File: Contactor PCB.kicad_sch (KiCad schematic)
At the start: 21 parts, among them J1 TSCU, J2 TSCU, J3 IMD, J4 AIL, J5 UIL, J6 TBD, J7 To Precharge, U1 Gigavac_GX21CAB, U2 Gigavac_GX21CAB

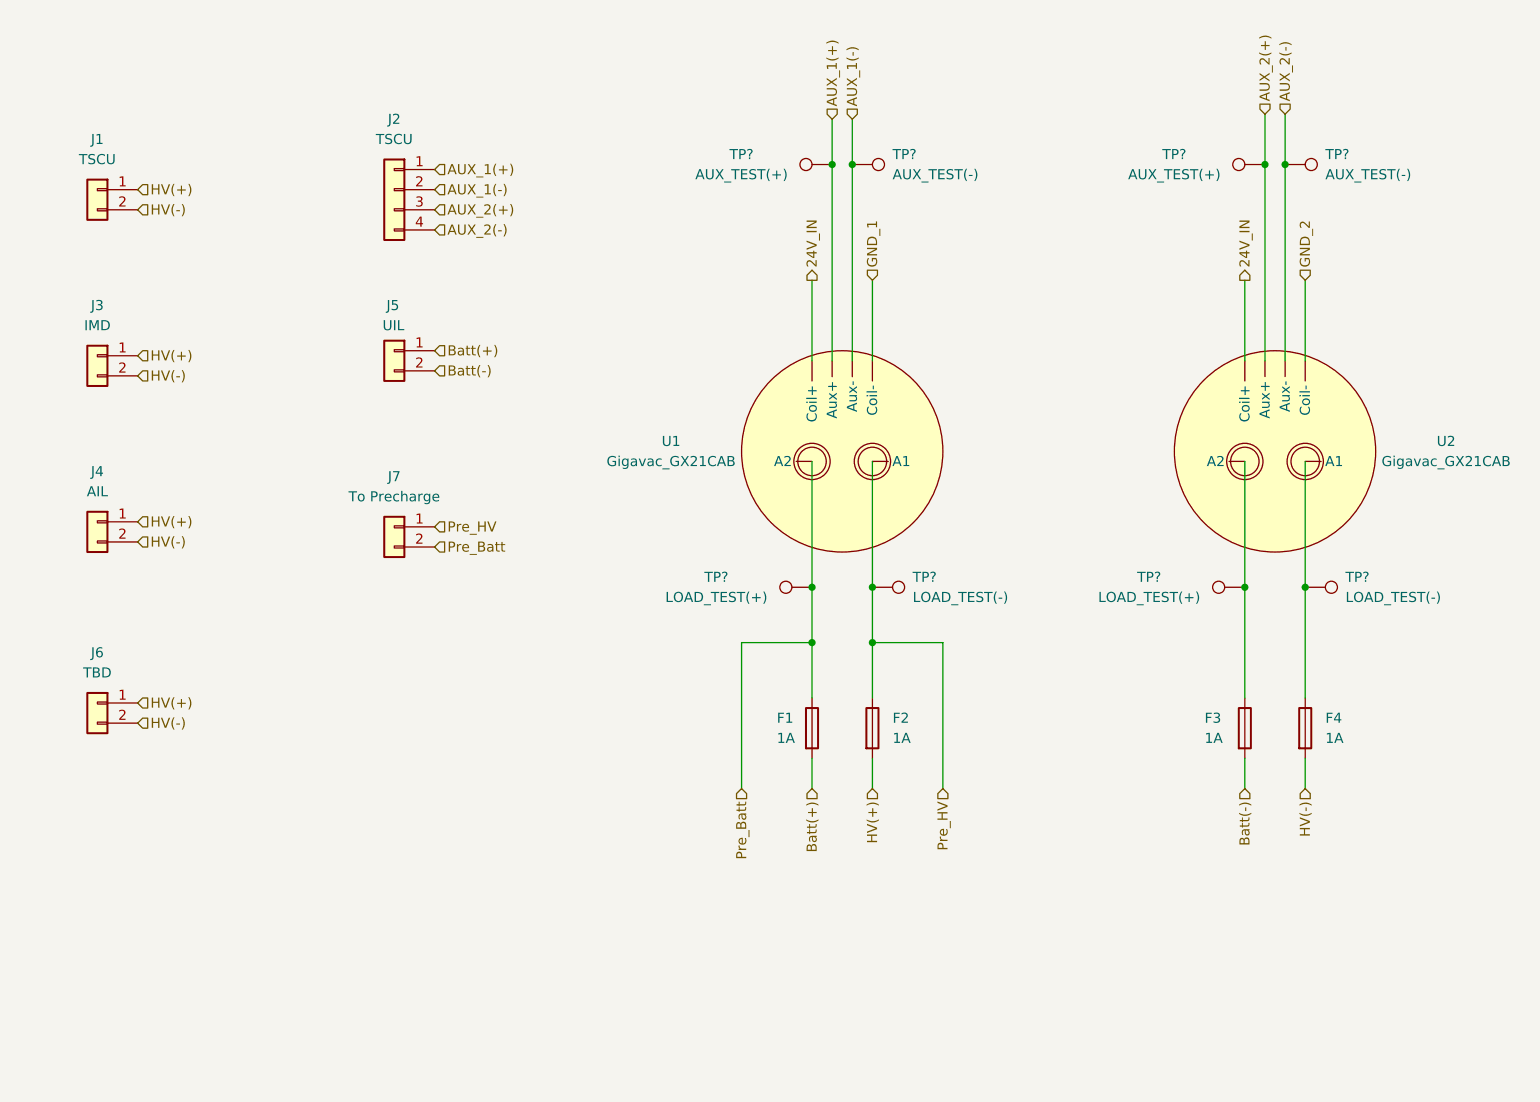
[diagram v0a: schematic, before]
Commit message: Added layout first draft
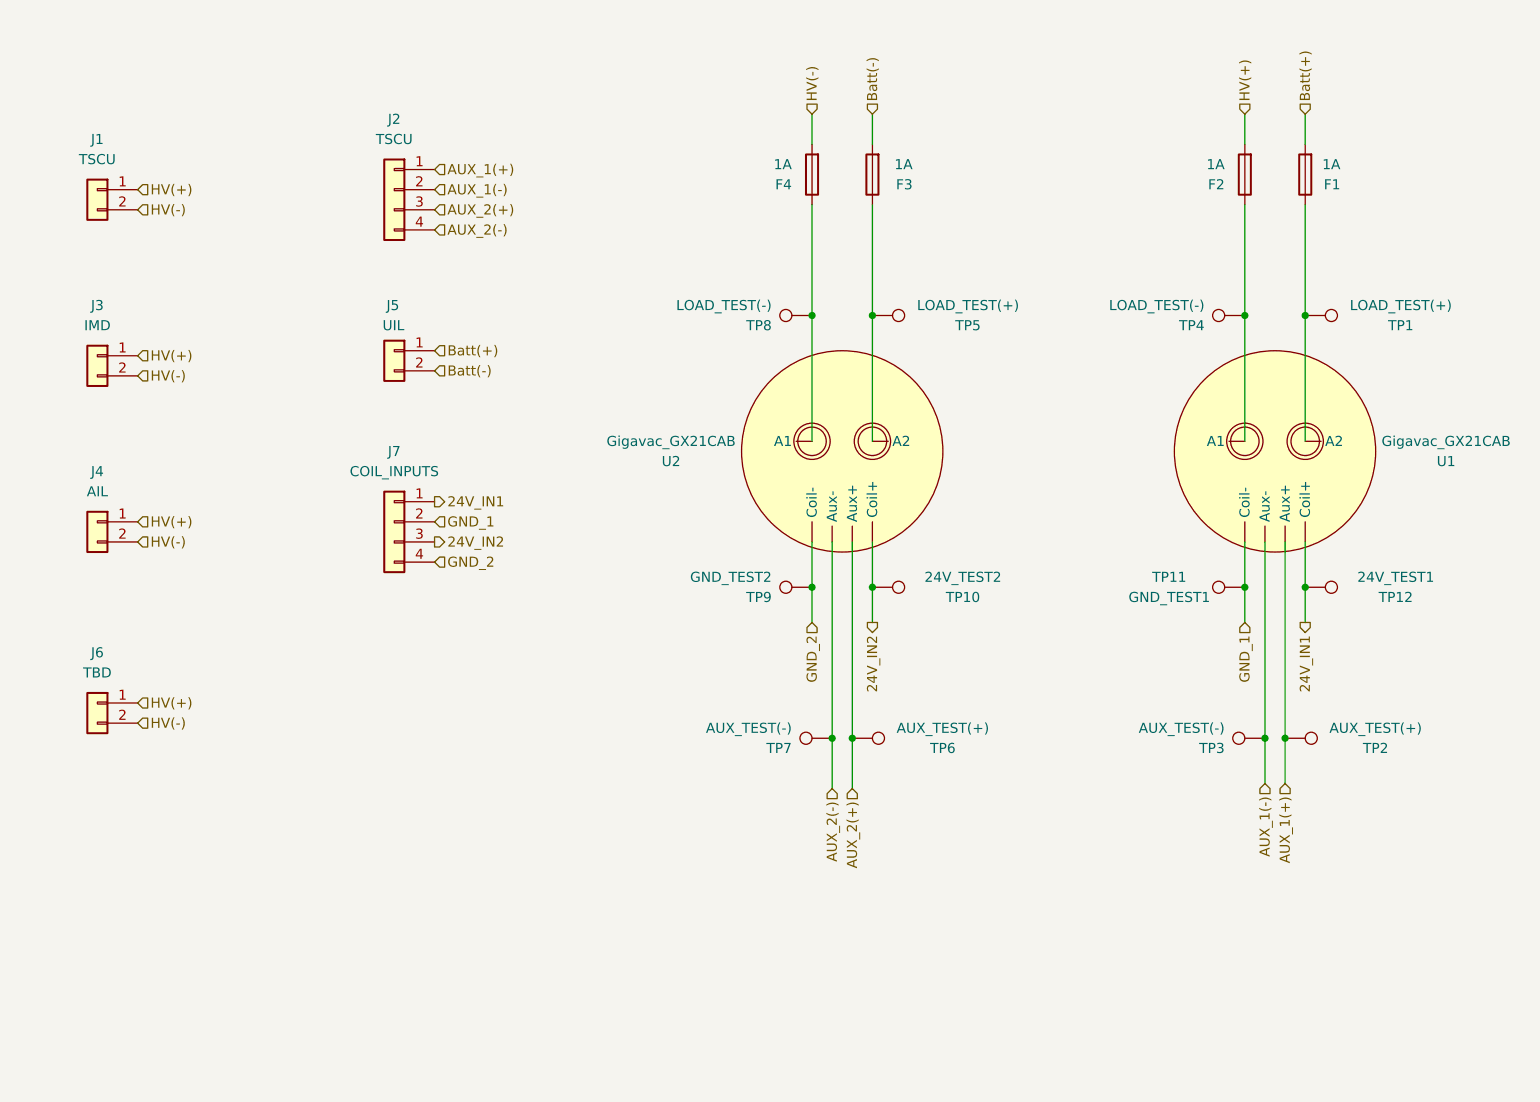
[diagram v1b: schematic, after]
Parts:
- removed J7: To Precharge, Connector_Molex:Molex_Micro-Fit_3.0_43045-0200_2x01_P3.00mm_Horizontal, symbol Connector_Generic:Conn_01x02
- added J7: COIL_INPUTS, Connector_Molex:Molex_Micro-Fit_3.0_43045-0400_2x02_P3.00mm_Horizontal, symbol Connector_Generic:Conn_01x04
- added TP10: 24V_TEST2, TestPoint:TestPoint_THTPad_D1.0mm_Drill0.5mm, symbol Connector:TestPoint
- added TP11: GND_TEST1, TestPoint:TestPoint_THTPad_D1.0mm_Drill0.5mm, symbol Connector:TestPoint
- added TP12: 24V_TEST1, TestPoint:TestPoint_THTPad_D1.0mm_Drill0.5mm, symbol Connector:TestPoint
- added TP9: GND_TEST2, TestPoint:TestPoint_THTPad_D1.0mm_Drill0.5mm, symbol Connector:TestPoint
- J1: footprint Connector_Molex:Molex_Micro-Fit_3.0_43045-0600_2x03_P3.00mm_Horizontal -> Connector_Molex:Molex_Micro-Fit_3.0_43045-0200_2x01_P3.00mm_Horizontal
- TP1, TP2, TP3, TP4, TP5, TP6, TP7, TP8: renamed from TP?; footprint (none) -> TestPoint:TestPoint_THTPad_D1.0mm_Drill0.5mm
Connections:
- net GND_1: now also J7.2 (Pin_2), TP11.1
- net GND_2: now also J7.4 (Pin_4), TP9.1
- removed net 24V_IN: U1. (Coil-), U2. (Coil-)
- net Pre_Batt: no longer names the net of F1.1, TP1.1, U1. (Coil-)
- net Pre_HV: no longer names the net of F2.1, TP4.1, U1. (Coil-)
- new net 24V_IN1: J7.1 (Pin_1), TP12.1, U1. (Coil-)
- new net 24V_IN2: J7.3 (Pin_3), TP10.1, U2. (Coil-)
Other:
- moved on the sheet: F1, F2, F3, F4, TP1, TP2, TP3, TP4, TP5, TP6, TP7, TP8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

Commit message: Condensed Version
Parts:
- added J10: COIL2_CONNECTOR, Connector_Molex:Molex_Micro-Fit_3.0_43045-0212_2x01_P3.00mm_Vertical, symbol Connector_Generic:Conn_01x02
- added J11: AUX2_CONNECTOR, Connector_Molex:Molex_Micro-Fit_3.0_43045-0212_2x01_P3.00mm_Vertical, symbol Connector_Generic:Conn_01x02
- added J8: COIL1_CONNECTOR, Connector_Molex:Molex_Micro-Fit_3.0_43045-0212_2x01_P3.00mm_Vertical, symbol Connector_Generic:Conn_01x02
- added J9: AUX1_CONNECTOR, Connector_Molex:Molex_Micro-Fit_3.0_43045-0212_2x01_P3.00mm_Vertical, symbol Connector_Generic:Conn_01x02
- J1, J3, J4, J5, J6: footprint Connector_Molex:Molex_Micro-Fit_3.0_43045-0200_2x01_P3.00mm_Horizontal -> Connector_Molex:Molex_Micro-Fit_3.0_43045-0212_2x01_P3.00mm_Vertical
- J2, J7: footprint Connector_Molex:Molex_Micro-Fit_3.0_43045-0400_2x02_P3.00mm_Horizontal -> Connector_Molex:Molex_Micro-Fit_3.0_43045-0412_2x02_P3.00mm_Vertical
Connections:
- net 24V_IN1: now also J8.1 (Pin_1)
- net 24V_IN2: now also J10.1 (Pin_1)
- net AUX_1(+): now also J9.1 (Pin_1)
- net AUX_1(-): now also J9.2 (Pin_2)
- net AUX_2(+): now also J11.1 (Pin_1)
- net AUX_2(-): now also J11.2 (Pin_2)
- net Batt(+): now also J5.2 (Pin_2); no longer J5.1 (Pin_1)
- net Batt(-): now also J5.1 (Pin_1); no longer J5.2 (Pin_2)
- net GND_1: now also J8.2 (Pin_2)
- net GND_2: now also J10.2 (Pin_2)
- net HV(+): now also J1.2 (Pin_2), J3.2 (Pin_2), J4.2 (Pin_2), J6.2 (Pin_2); no longer J1.1 (Pin_1), J3.1 (Pin_1), J4.1 (Pin_1), J6.1 (Pin_1)
- net HV(-): now also J1.1 (Pin_1), J3.1 (Pin_1), J4.1 (Pin_1), J6.1 (Pin_1); no longer J1.2 (Pin_2), J3.2 (Pin_2), J4.2 (Pin_2), J6.2 (Pin_2)
- net at F4.1, TP8.1: now also U2.1 (A1); no longer U2. (Coil-)
- net at F3.1, TP5.1: now also U2.2 (A2); no longer U2. (Coil-)
- net at F2.1, TP4.1: now also U1.1 (A1); no longer U1. (Coil-)
- net at F1.1, TP1.1: now also U1.2 (A2); no longer U1. (Coil-)

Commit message: Finalize Board
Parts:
- removed J1: TSCU, Connector_Molex:Molex_Micro-Fit_3.0_43045-0212_2x01_P3.00mm_Vertical, symbol Connector_Generic:Conn_01x02
- removed J10: COIL2_CONNECTOR, Connector_Molex:Molex_Micro-Fit_3.0_43045-0212_2x01_P3.00mm_Vertical, symbol Connector_Generic:Conn_01x02
- removed J11: AUX2_CONNECTOR, Connector_Molex:Molex_Micro-Fit_3.0_43045-0212_2x01_P3.00mm_Vertical, symbol Connector_Generic:Conn_01x02
- removed J2: TSCU, Connector_Molex:Molex_Micro-Fit_3.0_43045-0412_2x02_P3.00mm_Vertical, symbol Connector_Generic:Conn_01x04
- removed J3: IMD, Connector_Molex:Molex_Micro-Fit_3.0_43045-0212_2x01_P3.00mm_Vertical, symbol Connector_Generic:Conn_01x02
- removed J4: AIL, Connector_Molex:Molex_Micro-Fit_3.0_43045-0212_2x01_P3.00mm_Vertical, symbol Connector_Generic:Conn_01x02
- removed J5: UIL, Connector_Molex:Molex_Micro-Fit_3.0_43045-0212_2x01_P3.00mm_Vertical, symbol Connector_Generic:Conn_01x02
- removed J6: TBD, Connector_Molex:Molex_Micro-Fit_3.0_43045-0212_2x01_P3.00mm_Vertical, symbol Connector_Generic:Conn_01x02
- removed J7: COIL_INPUTS, Connector_Molex:Molex_Micro-Fit_3.0_43045-0412_2x02_P3.00mm_Vertical, symbol Connector_Generic:Conn_01x04
- removed J8: COIL1_CONNECTOR, Connector_Molex:Molex_Micro-Fit_3.0_43045-0212_2x01_P3.00mm_Vertical, symbol Connector_Generic:Conn_01x02
- removed J9: AUX1_CONNECTOR, Connector_Molex:Molex_Micro-Fit_3.0_43045-0212_2x01_P3.00mm_Vertical, symbol Connector_Generic:Conn_01x02
- removed TP10: 24V_TEST2, TestPoint:TestPoint_THTPad_D1.0mm_Drill0.5mm, symbol Connector:TestPoint
- removed TP11: GND_TEST1, TestPoint:TestPoint_THTPad_D1.0mm_Drill0.5mm, symbol Connector:TestPoint
- removed TP12: 24V_TEST1, TestPoint:TestPoint_THTPad_D1.0mm_Drill0.5mm, symbol Connector:TestPoint
- removed TP2, TP6: AUX_TEST(+), TestPoint:TestPoint_THTPad_D1.0mm_Drill0.5mm, symbol Connector:TestPoint
- removed TP3, TP7: AUX_TEST(-), TestPoint:TestPoint_THTPad_D1.0mm_Drill0.5mm, symbol Connector:TestPoint
- removed TP9: GND_TEST2, TestPoint:TestPoint_THTPad_D1.0mm_Drill0.5mm, symbol Connector:TestPoint
- added J1: HV Connector, Connector_Molex:Molex_Micro-Fit_3.0_43045-1012_2x05_P3.00mm_Vertical, symbol Connector_Generic:Conn_02x05_Top_Bottom
- added J2: Batt Connector, Connector_Molex:Molex_Micro-Fit_3.0_43045-0612_2x03_P3.00mm_Vertical, symbol Connector_Generic:Conn_02x03_Top_Bottom
- F1, F2, F3, F4: footprint CustomFootprints:Fuse_Placeholder -> CustomFootprints:0ADAP1000RE
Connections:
- net Batt(+): now also J2.1 (Pin_1), J2.2 (Pin_2), J2.3 (Pin_3)
- net Batt(-): now also J2.4 (Pin_4), J2.5 (Pin_5), J2.6 (Pin_6)
- net HV(+): now also J1.1 (Pin_1), J1.2 (Pin_2), J1.3 (Pin_3), J1.4 (Pin_4), J1.5 (Pin_5)
- net HV(-): now also J1.10 (Pin_10), J1.6 (Pin_6), J1.7 (Pin_7), J1.8 (Pin_8), J1.9 (Pin_9)
- net at F2.1, TP4.1: now also U1.2 (A2); no longer U1.1 (A1)
- net at F1.1, TP1.1: now also U1.1 (A1); no longer U1.2 (A2)
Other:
- moved on the sheet: F1, F2, TP1, TP4
